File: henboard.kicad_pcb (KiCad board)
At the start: 2 copper layers, 0 parts

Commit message: Finish piano
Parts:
- added J1: Conn_01x22, Connector_PinHeader_2.54mm:PinHeader_1x22_P2.54mm_Vertical, F.Cu at (114.3, 81.3)
- added J10: Conn_01x01, Pad-CapacitiveTouch:Pad-CapacitiveTouch-small, F.Cu at (60.0, 190.0)
- added J11: Conn_01x01, Pad-CapacitiveTouch:Pad-CapacitiveTouch-small, F.Cu at (75.0, 190.0)
- added J12: Conn_01x01, Pad-CapacitiveTouch:Pad-CapacitiveTouch-small, F.Cu at (90.0, 190.0)
- added J13: Conn_01x01, Pad-CapacitiveTouch:Pad-CapacitiveTouch-small, F.Cu at (105.0, 190.0)
- added J14: Conn_01x01, Pad-CapacitiveTouch:Pad-CapacitiveTouch-small, F.Cu at (115.0, 190.0)
- added J15: Conn_01x01, Pad-CapacitiveTouch:Pad-CapacitiveTouch-small, B.Cu at (138.7, 115.0)
- added J16: Conn_01x01, Pad-CapacitiveTouch:Pad-CapacitiveTouch-small, F.Cu at (130.0, 190.0)
- added J17: Conn_01x01, Pad-CapacitiveTouch:Pad-CapacitiveTouch-small, F.Cu at (145.0, 190.0)
- added J18: Conn_01x01, Pad-CapacitiveTouch:Pad-CapacitiveTouch-small, F.Cu at (132.5, 124.0)
- added J19: Conn_01x01, Pad-CapacitiveTouch:Pad-CapacitiveTouch-small, F.Cu at (155.0, 190.0)
- added J2: Conn_01x22, Connector_PinHeader_2.54mm:PinHeader_1x22_P2.54mm_Vertical, F.Cu at (114.3, 58.4)
- added J20: Conn_01x01, Pad-CapacitiveTouch:Pad-CapacitiveTouch-small, F.Cu at (170.0, 190.0)
- added J21: Conn_01x01, Pad-CapacitiveTouch:Pad-CapacitiveTouch-small, F.Cu at (147.9, 126.1)
- added J22: Conn_01x01, Pad-CapacitiveTouch:Pad-CapacitiveTouch-small, F.Cu at (147.9, 128.1)
- added J3: Conn_01x01, Pad-CapacitiveTouch:Pad-CapacitiveTouch-small, F.Cu at (96.8, 126.8)
- added J4: Conn_01x01, Pad-CapacitiveTouch:Pad-CapacitiveTouch-small, F.Cu at (96.8, 128.8)
- added J5: Conn_01x01, Pad-CapacitiveTouch:Pad-CapacitiveTouch-small, F.Cu at (20.0, 190.0)
- added J6: Conn_01x01, Pad-CapacitiveTouch:Pad-CapacitiveTouch-small, F.Cu at (35.0, 190.0)
- added J7: Conn_01x01, Pad-CapacitiveTouch:Pad-CapacitiveTouch-small, F.Cu at (50.0, 190.0)
- added J8: Conn_01x01, Pad-CapacitiveTouch:Pad-CapacitiveTouch-small, F.Cu at (108.2, 123.9)
- added J9: Conn_01x01, Pad-CapacitiveTouch:Pad-CapacitiveTouch-small, B.Cu at (105.8, 114.8)
- added S1: SKRPACE010, SKRPACE010:SKRPACE010, F.Cu at (125.8, 25.7)
- added S2: SKRPACE010, SKRPACE010:SKRPACE010, F.Cu at (131.5, 25.7)
- added S3: SKRPACE010, SKRPACE010:SKRPACE010, F.Cu at (137.2, 25.7)
- added S4: SKRPACE010, SKRPACE010:SKRPACE010, F.Cu at (142.9, 25.7)
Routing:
- added copper zone on F.Cu, net TOUCH1
- added copper zone on F.Cu, net TOUCH10
- added copper zone on F.Cu, net TOUCH11
- added copper zone on F.Cu, net TOUCH12
- added copper zone on F.Cu, net TOUCH13
- added copper zone on F.Cu, net TOUCH14
- added copper zone on F.Cu, net TOUCH2
- added copper zone on F.Cu, net TOUCH4
- added copper zone on F.Cu, net TOUCH5
- added copper zone on F.Cu, net TOUCH6
- added copper zone on F.Cu, net TOUCH7
- added copper zone on F.Cu, net TOUCH9

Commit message: Finish all
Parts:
- moved J22 233.4 mm to (377.0, 172.5)
- moved J21 219.1 mm to (367.0, 122.0)
- moved J7 215.6 mm to (240.9, 90.0)
- moved J5 213.4 mm to (208.9, 90.7)
- moved J15 210.0 mm to (339.0, 52.0)
- moved J18 209.4 mm to (335.8, 74.0)
- moved J19 207.9 mm to (341.8, 98.7)
- moved J20 207.1 mm to (351.8, 90.7)
- moved J6 205.4 mm to (218.9, 98.7)
- moved J11 202.5 mm to (265.7, 122.0)
- moved J10 201.5 mm to (249.7, 122.0)
- moved J17 201.4 mm to (319.8, 90.0)
- moved J16 194.3 mm to (312.1, 122.0)
- moved J14 193.7 mm to (296.4, 122.0)
- moved J12 193.1 mm to (270.7, 122.0)
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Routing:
- net TOUCH8: track 0.00 -> 483.8 mm, vias 0 -> 2
- net TOUCH3: track 0.00 -> 395.0 mm
- net GND: track 0.00 -> 165.2 mm, vias 0 -> 3
- net TOUCH11: track 0.00 -> 120.4 mm, vias 0 -> 2
- net TOUCH5: track 0.00 -> 114.3 mm, vias 0 -> 2
- net TOUCH1: track 0.00 -> 87.5 mm
- net TOUCH2: track 0.00 -> 84.4 mm, vias 0 -> 1
- net TOUCH14: track 0.00 -> 75.3 mm
- net TOUCH9: track 0.00 -> 68.8 mm
- net TOUCH10: track 0.00 -> 68.4 mm
- net TOUCH7: track 0.00 -> 67.2 mm
- net TOUCH6: track 0.00 -> 66.5 mm
- net TOUCH13: track 0.00 -> 65.4 mm, vias 0 -> 1
- net TOUCH12: track 0.00 -> 44.0 mm
- net TOUCH4: track 0.00 -> 42.6 mm
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- added copper zone on B.Cu, net TOUCH11
- added copper zone on F.Cu, net TOUCH3
- added copper zone on B.Cu, net TOUCH5
- added copper zone on F.Cu, net TOUCH8
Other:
- board outline added: 200 x 200 mm

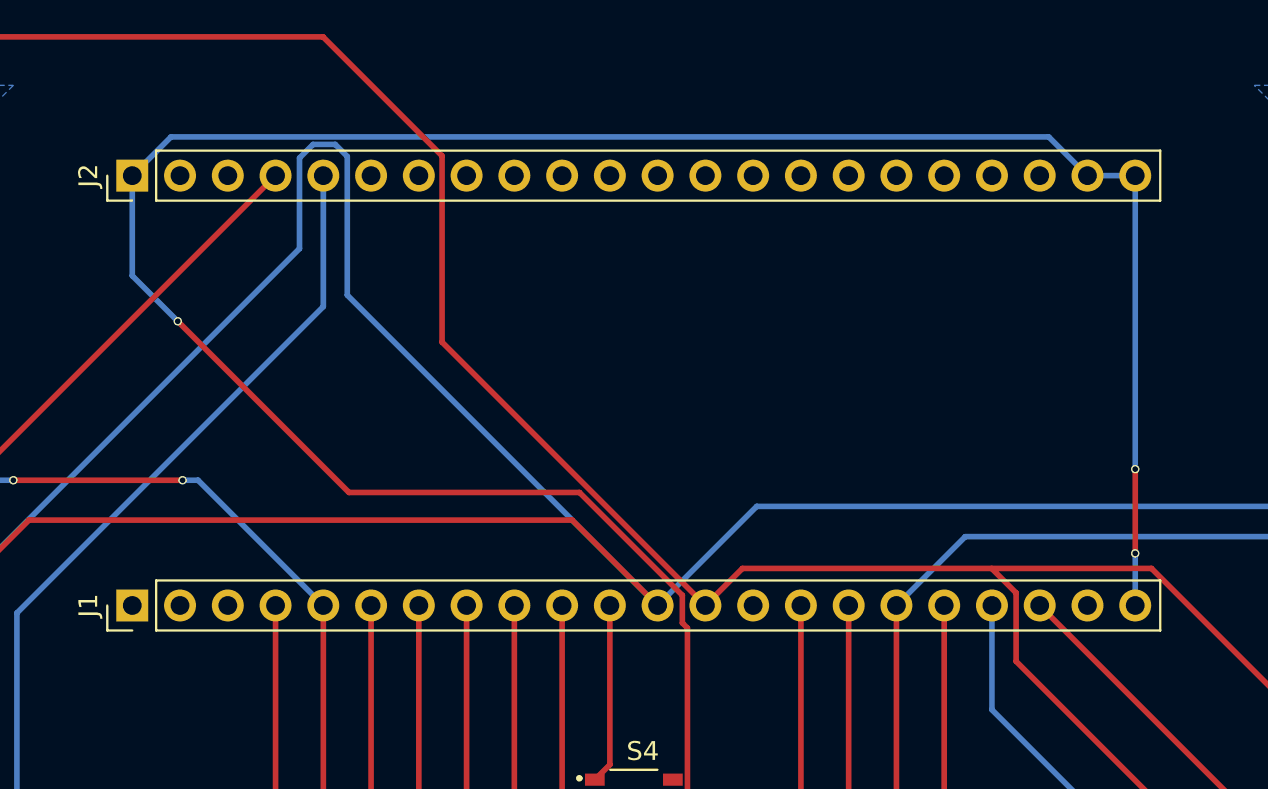
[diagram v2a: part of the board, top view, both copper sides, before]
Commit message: Add Silkscreen to be able to identify board direction
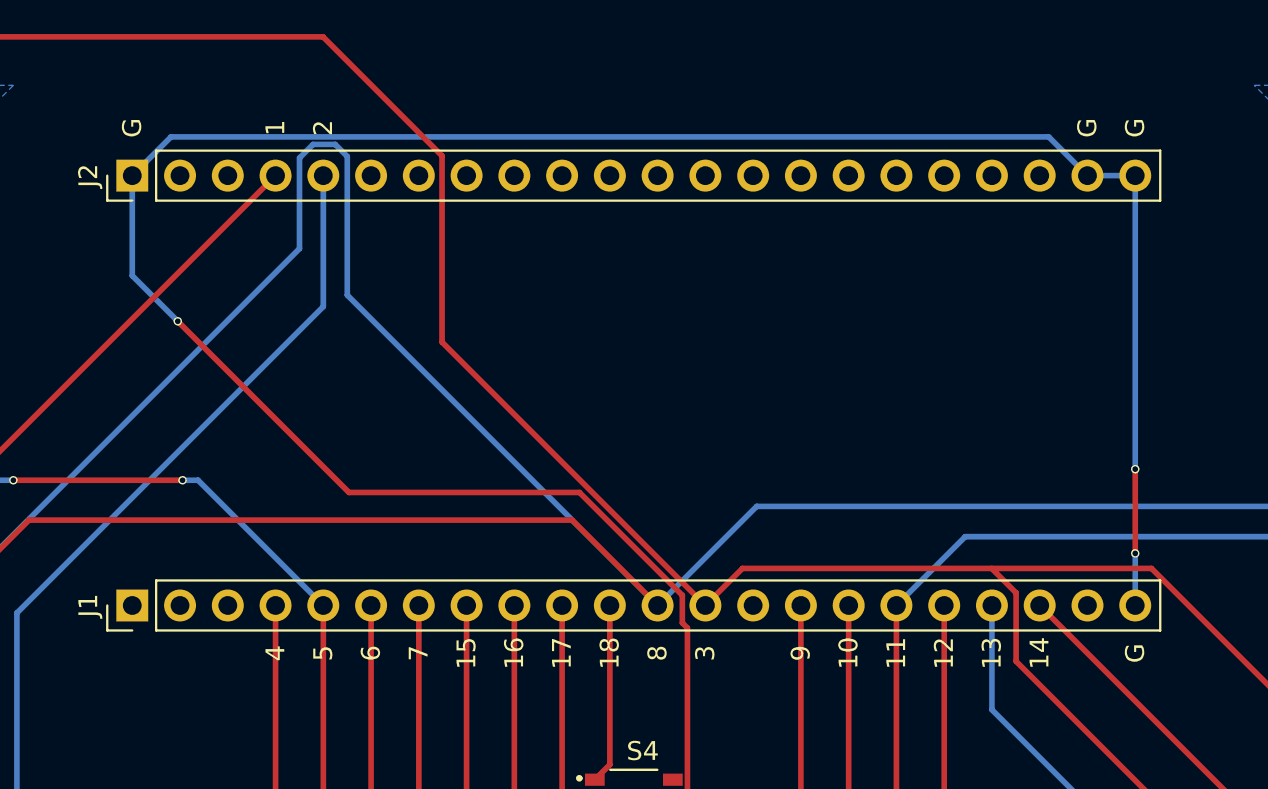
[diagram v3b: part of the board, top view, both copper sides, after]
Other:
- board text added: "1"
- board text added: "10"
- board text added: "11"
- board text added: "12"
- board text added: "13"
- board text added: "14"
- board text added: "15"
- board text added: "16"
- board text added: "17"
- board text added: "18"
- board text added: "2"
- board text added: "3"
- board text added: "4"
- board text added: "5"
- board text added: "6"
- board text added: "7"
- board text added: "8"
- board text added: "9"
- board text added: "G"
